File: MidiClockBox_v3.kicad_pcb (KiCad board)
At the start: 2 copper layers, 119.4 x 59.6 mm, 58 parts, among them J1 Midi In 0, J10 Display, J11 Midi Out 3, J12 Midi Out 4, J13 Midi Out 5, J14 Sync Out 0, J15 Sync Out 1, J2 ICSP, J3 Conn_02x09_Odd_Even, J4 Conn_02x04_Odd_Even, J5 Conn_02x12_Counter_Clockwise, J6 Midi Out 0, J7 Midi Out 1, J8 Midi Out 2, J9 WS2812, SW1 RotaryEncoder_Switch, U1 CD74HC4067SM, U2 74LS241, U3 6N138

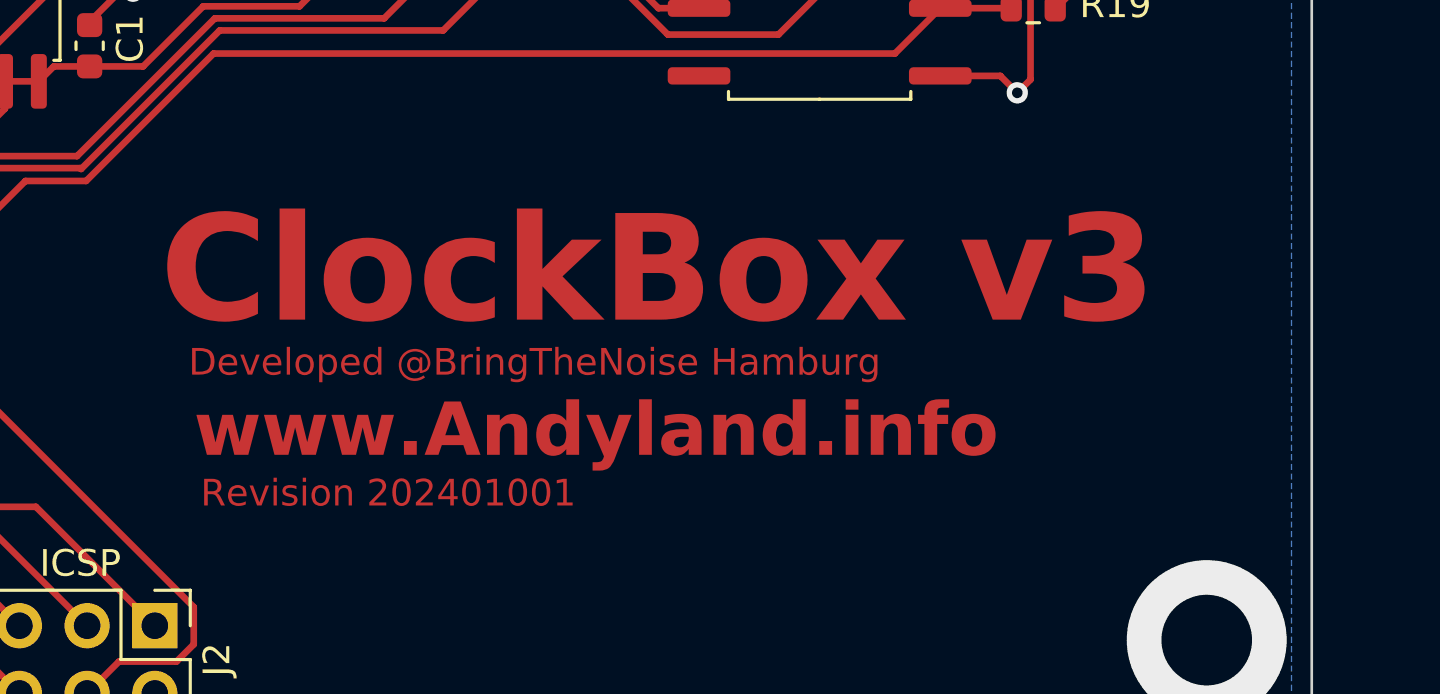
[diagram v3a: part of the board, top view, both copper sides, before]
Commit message: move logo to front silkscreen
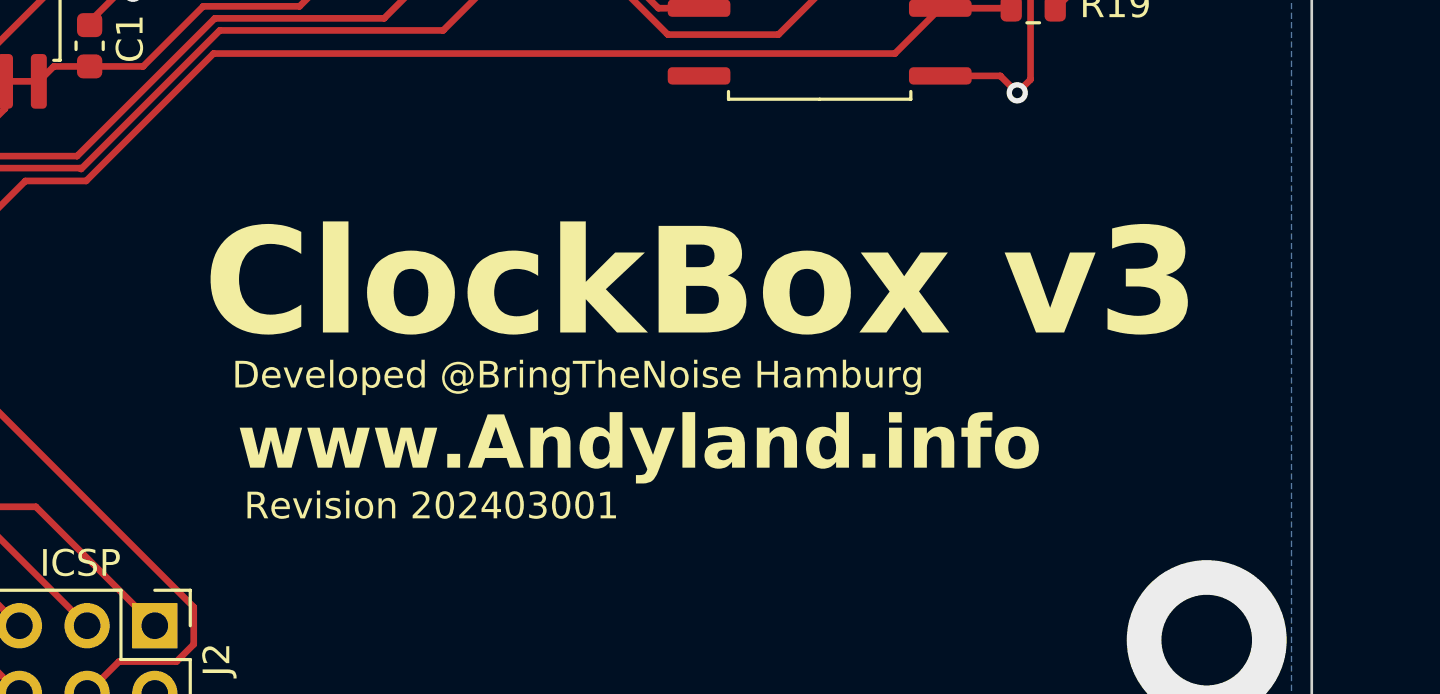
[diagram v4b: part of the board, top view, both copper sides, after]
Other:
- board text added: "Revision 202403001"
- board text removed: "Revision 202401001"
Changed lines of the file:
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@@
   (gr_rect (start 51.533056 43.813641) (end 170.938818 103.435608)
     (stroke (width 0.1) (type default)) (fill none) (layer "Edge.Cuts"))
-  (gr_text "ClockBox v3" (at 127.732337 86.46803) (layer "F.Cu")
+  (gr_text "Pre3" (at 73.914 66.675 45) (layer "F.SilkS")
+    (effects (font (size 1 1) (thickness 0.15)) (justify left bottom))
+  )
+  (gr_text "MidiOut 5" (at 73.406 61.595 90) (layer "F.SilkS")
+    (effects (font (size 1 1) (thickness 0.15)) (justify left bottom))
+  )
+  (gr_text "Display" (at 136.3218 65.659) (layer "F.SilkS")
+    (effects (font (size 1 1) (thickness 0.15)) (justify left bottom))
+  )
+  (gr_text "www.Andyland.info" (at 130.627937 91.77663) (layer "F.SilkS")
+    (effects (font (size 2 2) (thickness 0.5) bold) (justify left bottom))
+  )
+  (gr_text "SCL" (at 139.192 73.279 90) (layer "F.SilkS")
+    (effects (font (size 1 1) (thickness 0.15)) (justify left bottom))
+  )
+  (gr_text "MidiOut 4" (at 61.722 61.468 90) (layer "F.SilkS")
+    (effects (font (size 1 1) (thickness 0.15)) (justify left bottom))
+  )
+  (gr_text "SyncOut 0" (at 130.302 60.96 90) (layer "F.SilkS")
+    (effects (font (size 1 1) (thickness 0.15)) (justify left bottom))
+  )
+  (gr_text "SDA" (at 141.478 73.152 90) (layer "F.SilkS")
+    (effects (font (size 1 1) (thickness 0.15)) (justify left bottom))
+  )
+  (gr_text "Tap" (at 61.722 66.802 45) (layer "F.SilkS")
+    (effects (font (size 1 1) (thickness 0.15)) (justify left bottom))
+  )
+  (gr_text "FSW1" (at 76.454 66.675 45) (layer "F.SilkS")
+    (effects (font (size 1 1) (thickness 0.15)) (justify left bottom))
+  )
+  (gr_text "Start" (at 64.389 66.802 45) (layer "F.SilkS")
+    (effects (font (size 1 1) (thickness 0.15)) (justify left bottom))
+  )
+  (gr_text "WS2812" (at 58.6232 85.6742 90) (layer "F.SilkS")
+    (effects (font (size 1 1) (thickness 0.15)) (justify left bottom))
+  )
+  (gr_text "MidiIn" (at 153.416 60.706 90) (layer "F.SilkS")
+    (effects (font (size 1 1) (thickness 0.15)) (justify left bottom))
+  )
+  (gr_text "GND" (at 133.985 73.279 90) (layer "F.SilkS")
+    (effects (font (size 1 1) (thickness 0.15)) (justify left bottom))
+  )
+  (gr_text "Pre2" (at 71.374 66.675 45) (layer "F.SilkS")
+    (effects (font (size 1 1) (thickness 0.15)) (justify left bottom))
+  )
+  (gr_text "MidiOut 0" (at 119.126 61.214 90) (layer "F.SilkS")
+    (effects (font (size 1 1) (thickness 0.15)) (justify left bottom))
+  )
+  (gr_text "Pre1" (at 69.215 66.675 45) (layer "F.SilkS")
+    (effects (font (size 1 1) (thickness 0.15)) (justify left bottom))
+  )
+  (gr_text "MidiOut 2" (at 96.139 61.341 90) (layer "F.SilkS")
+    (effects (font (size 1 1) (thickness 0.15)) (justify left bottom))
+  )
+  (gr_text "Stop" (at 67.056 66.675 45) (layer "F.SilkS")
+    (effects (font (size 1 1) (thickness 0.15)) (justify left bottom))
+  )
+  (gr_text "ClockBox v3" (at 129.357937 86.95063) (layer "F.SilkS")
     (effects (font (size 4 4) (thickness 1) bold) (justify left bottom))
   )
-  (gr_text "www.Andyland.info" (at 129.002337 91.29403) (layer "F.Cu")
-    (effects (font (size 2 2) (thickness 0.5) bold) (justify left bottom))
-  )
-  (gr_text "Developed @BringTheNoise Hamburg" (at 128.8034 88.1634) (layer "F.Cu")
-    (effects (font (size 1 1) (thickness 0.15)) (justify left bottom))
-  )
-  (gr_text "Revision 202401001" (at 129.256337 93.07203) (layer "F.Cu")
+  (gr_text "Vcc" (at 136.398 73.152 90) (layer "F.SilkS")
+    (effects (font (size 1 1) (thickness 0.15)) (justify left bottom))
+  )
+  (gr_text "In 15 11 10 9" (at 59 102) (layer "F.SilkS")
+    (effects (font (size 1 1) (thickness 0.15)) (justify left bottom))
+  )
+  (gr_text "FSW3" (at 81.915 66.675 45) (layer "F.SilkS")
+    (effects (font (size 1 1) (thickness 0.15)) (justify left bottom))
+  )
+  (gr_text "Revision 202403001" (at 130.881937 93.55463) (layer "F.SilkS")
     (effects (font (size 1 1) (thickness 0.125)) (justify left bottom))
   )
-  (gr_text "Pre3" (at 73.914 66.675 45) (layer "F.SilkS")
-    (effects (font (size 1 1) (thickness 0.15)) (justify left bottom))
-  )
-  (gr_text "MidiOut 5" (at 73.406 61.595 90) (layer "F.SilkS")
-    (effects (font (size 1 1) (thickness 0.15)) (justify left bottom))
-  )
-  (gr_text "Display" (at 136.3218 65.659) (layer "F.SilkS")
-    (effects (font (size 1 1) (thickness 0.15)) (justify left bottom))
-  )
-  (gr_text "SCL" (at 139.192 73.279 90) (layer "F.SilkS")
-    (effects (font (size 1 1) (thickness 0.15)) (justify left bottom))
-  )
-  (gr_text "MidiOut 4" (at 61.722 61.468 90) (layer "F.SilkS")
-    (effects (font (size 1 1) (thickness 0.15)) (justify left bottom))
-  )
-  (gr_text "SyncOut 0" (at 130.302 60.96 90) (layer "F.SilkS")
-    (effects (font (size 1 1) (thickness 0.15)) (justify left bottom))
-  )
-  (gr_text "SDA" (at 141.478 73.152 90) (layer "F.SilkS")
-    (effects (font (size 1 1) (thickness 0.15)) (justify left bottom))
-  )
-  (gr_text "Tap" (at 61.722 66.802 45) (layer "F.SilkS")
-    (effects (font (size 1 1) (thickness 0.15)) (justify left bottom))
-  )
-  (gr_text "FSW1" (at 76.454 66.675 45) (layer "F.SilkS")
-    (effects (font (size 1 1) (thickness 0.15)) (justify left bottom))
-  )
-  (gr_text "Start" (at 64.389 66.802 45) (layer "F.SilkS")
-    (effects (font (size 1 1) (thickness 0.15)) (justify left bottom))
-  )
-  (gr_text "WS2812" (at 58.6232 85.6742 90) (layer "F.SilkS")
-    (effects (font (size 1 1) (thickness 0.15)) (justify left bottom))
-  )
-  (gr_text "MidiIn" (at 153.416 60.706 90) (layer "F.SilkS")
-    (effects (font (size 1 1) (thickness 0.15)) (justify left bottom))
-  )
-  (gr_text "GND" (at 133.985 73.279 90) (layer "F.SilkS")
-    (effects (font (size 1 1) (thickness 0.15)) (justify left bottom))
-  )
-  (gr_text "Pre2" (at 71.374 66.675 45) (layer "F.SilkS")
-    (effects (font (size 1 1) (thickness 0.15)) (justify left bottom))
-  )
-  (gr_text "MidiOut 0" (at 119.126 61.214 90) (layer "F.SilkS")
-    (effects (font (size 1 1) (thickness 0.15)) (justify left bottom))
-  )
-  (gr_text "Pre1" (at 69.215 66.675 45) (layer "F.SilkS")
-    (effects (font (size 1 1) (thickness 0.15)) (justify left bottom))
-  )
-  (gr_text "MidiOut 2" (at 96.139 61.341 90) (layer "F.SilkS")
-    (effects (font (size 1 1) (thickness 0.15)) (justify left bottom))
-  )
-  (gr_text "Stop" (at 67.056 66.675 45) (layer "F.SilkS")
-    (effects (font (size 1 1) (thickness 0.15)) (justify left bottom))
-  )
-  (gr_text "Vcc" (at 136.398 73.152 90) (layer "F.SilkS")
-    (effects (font (size 1 1) (thickness 0.15)) (justify left bottom))
-  )
-  (gr_text "In 15 11 10 9" (at 59 102) (layer "F.SilkS")
-    (effects (font (size 1 1) (thickness 0.15)) (justify left bottom))
-  )
-  (gr_text "FSW3" (at 81.915 66.675 45) (layer "F.SilkS")
-    (effects (font (size 1 1) (thickness 0.15)) (justify left bottom))
-  )
   (gr_text "SyncOut 1" (at 141.859 60.833 90) (layer "F.SilkS")
     (effects (font (size 1 1) (thickness 0.15)) (justify left bottom))
   )
   (gr_text "MidiOut 3" (at 84.455 61.468 90) (layer "F.SilkS")
+    (effects (font (size 1 1) (thickness 0.15)) (justify left bottom))
+  )
+  (gr_text "Developed @BringTheNoise Hamburg" (at 130.429 88.646) (layer "F.SilkS")
     (effects (font (size 1 1) (thickness 0.15)) (justify left bottom))
   )
@@
     )
   )
-  (group "" (id 4647536a-94f9-48d1-9da8-8cbf230ba0d7)
-    (members
-      0ccb5f8d-aecf-4c1f-941a-b4503c0903b2
-      b15accea-f944-4657-8fa9-7baad0f6fbe5
-      bf546221-9e49-407b-92a5-5ecac96828be
-      cd3cfbac-6221-4ff0-b0d9-209cd6b0f6bc
-    )
-  )
   (group "" (id 8236fb1e-173b-4cd7-a7ce-d049ec6a13ec)
     (members
@@
     )
   )
+  (group "" (id e09b6506-b82b-4535-acfe-793dc9e83ec3)
+    (members
+      173d98b1-d087-4f87-98a6-acae7db6542c
+      ab5ae065-d388-4755-836f-a2c5ee350eb7
+      c1510ebe-6fb2-4c0a-8b0c-e8ff4e965da0
+      e0b613d2-a6b5-4014-a314-85e267303443
+    )
+  )
